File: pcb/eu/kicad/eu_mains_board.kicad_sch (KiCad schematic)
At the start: 10 parts, among them J1 2604-3102, J2 2604-3102, J3 TSM-102-02-L-SV

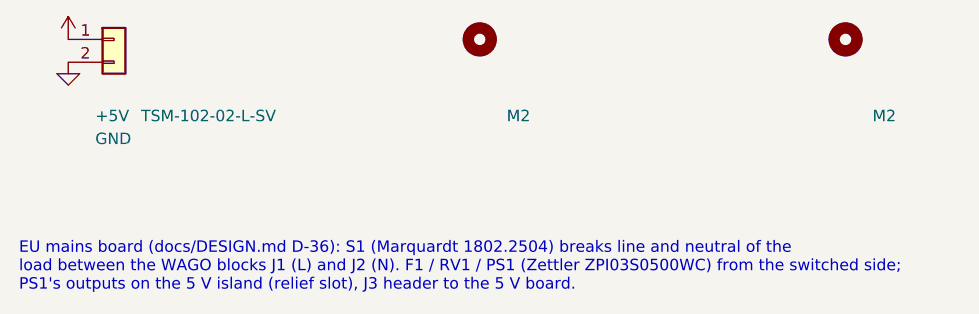
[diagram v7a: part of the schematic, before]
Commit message: Variants equal: na/eu/shared layout, shared part names, no default variant (D-125)
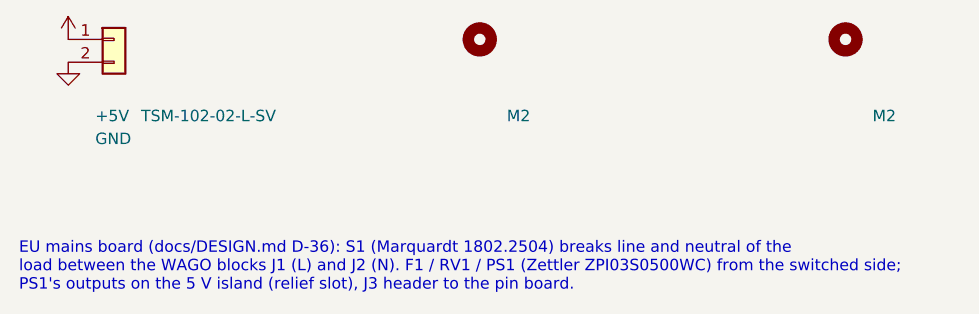
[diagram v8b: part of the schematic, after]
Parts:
- F1: footprint eu:Fuse_Schurter_UMT250 -> eu_mains:Fuse_Schurter_UMT250; symbol eu:Fuse -> eu_mains:Fuse
- J1, J2: footprint eu:WAGO_2604-3102_1x02_P5.00mm_Vertical -> eu_mains:WAGO_2604-3102_1x02_P5.00mm_Vertical; symbol eu:Screw_Terminal_01x02 -> eu_mains:Screw_Terminal_01x02
- J3: footprint eu:PinHeader_1x02_P2.54mm_Vertical_SMD_Pin1Left -> eu_mains:PinHeader_1x02_P2.54mm_Vertical_SMD_Pin1Left; symbol eu:Conn_01x02 -> eu_mains:Conn_01x02
- MH1, MH2, MH3: footprint eu:MountingHole_2.2mm_M2 -> eu_mains:MountingHole_2.2mm_M2; symbol eu:MountingHole -> eu_mains:MountingHole
- PS1: footprint eu:Converter_ACDC_Zettler_ZPI03_THT -> eu_mains:Converter_ACDC_Zettler_ZPI03_THT; symbol eu:ZPI03S0500WC -> eu_mains:ZPI03S0500WC
- RV1: footprint eu:Varistor_TDK_CU4032 -> eu_mains:Varistor_TDK_CU4032; symbol eu:Varistor -> eu_mains:Varistor
- S1: footprint eu:Rocker_DPST_Marquardt_1802.2504_E-Switch_RA412C1100 -> eu_mains:Rocker_DPST_Marquardt_1802.2504_E-Switch_RA412C1100; symbol eu:SW_DPST_Marquardt -> eu_mains:SW_DPST_Marquardt
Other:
- note added: "EU mains board (docs/DESIGN.md D-36): S1 (Marquardt 1802.2504) breaks line and neutral of the load between the WAGO blocks J1 (L) and J2 (N). F1 / RV1 / PS1 (Zettler ZPI03S0500WC) from the switched side; PS1's outputs on the 5 V island (relief slot), J3 header to the pin board."
- note removed: "EU mains board (docs/DESIGN.md D-36): S1 (Marquardt 1802.2504) breaks line and neutral of the load between the WAGO blocks J1 (L) and J2 (N). F1 / RV1 / PS1 (Zettler ZPI03S0500WC) from the switched side; PS1's outputs on the 5 V island (relief slot), J3 header to the 5 V board."
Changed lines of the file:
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@@
 		(rev "v0.6")
 		(company "smart-wallplate")
-		(comment 1 "Generated by pcb/eu/tools/gen_eu.py - edit eu_parts.py")
-	)
-	(symbol
-		(lib_id "eu:SW_DPST_Marquardt")
+		(comment 1 "Generated by pcb/eu/tools/gen_eu.py - edit parts_eu.py")
+	)
+	(symbol
+		(lib_id "eu_mains:SW_DPST_Marquardt")
 		(at 35.56 91.44 0)
 		(unit 1)
@@
 			)
 		)
-		(property "Footprint" "eu:Rocker_DPST_Marquardt_1802.2504_E-Switch_RA412C1100"
+		(property "Footprint" "eu_mains:Rocker_DPST_Marquardt_1802.2504_E-Switch_RA412C1100"
 			(at 35.56 91.44 0)
 			(effects
@@
 	)
 	(symbol
-		(lib_id "eu:Screw_Terminal_01x02")
+		(lib_id "eu_mains:Screw_Terminal_01x02")
 		(at 76.2 91.44 0)
 		(unit 1)
@@
 			)
 		)
-		(property "Footprint" "eu:WAGO_2604-3102_1x02_P5.00mm_Vertical"
+		(property "Footprint" "eu_mains:WAGO_2604-3102_1x02_P5.00mm_Vertical"
 			(at 76.2 91.44 0)
 			(effects
@@
 	)
 	(symbol
-		(lib_id "eu:Screw_Terminal_01x02")
+		(lib_id "eu_mains:Screw_Terminal_01x02")
 		(at 116.84 91.44 0)
 		(unit 1)
@@
 			)
 		)
-		(property "Footprint" "eu:WAGO_2604-3102_1x02_P5.00mm_Vertical"
+		(property "Footprint" "eu_mains:WAGO_2604-3102_1x02_P5.00mm_Vertical"
 			(at 116.84 91.44 0)
 			(effects
@@
 	)
 	(symbol
-		(lib_id "eu:Fuse")
+		(lib_id "eu_mains:Fuse")
 		(at 157.48 91.44 0)
 		(unit 1)
@@
 			)
 		)
-		(property "Footprint" "eu:Fuse_Schurter_UMT250"
+		(property "Footprint" "eu_mains:Fuse_Schurter_UMT250"
 			(at 157.48 91.44 0)
 			(effects
@@
 	)
 	(symbol
-		(lib_id "eu:Varistor")
+		(lib_id "eu_mains:Varistor")
 		(at 198.12 91.44 0)
 		(unit 1)
@@
 			)
 		)
-		(property "Footprint" "eu:Varistor_TDK_CU4032"
+		(property "Footprint" "eu_mains:Varistor_TDK_CU4032"
 			(at 198.12 91.44 0)
 			(effects
@@
 	)
 	(symbol
-		(lib_id "eu:ZPI03S0500WC")
+		(lib_id "eu_mains:ZPI03S0500WC")
 		(at 238.76 91.44 0)
 		(unit 1)
@@
 			)
 		)
-		(property "Footprint" "eu:Converter_ACDC_Zettler_ZPI03_THT"
+		(property "Footprint" "eu_mains:Converter_ACDC_Zettler_ZPI03_THT"
 			(at 238.76 91.44 0)
 			(effects
@@
 	)
 	(symbol
-		(lib_id "eu:+5V")
+		(lib_id "eu_mains:+5V")
 		(at 248.92 88.9 0)
 		(unit 1)
@@
 	)
 	(symbol
-		(lib_id "eu:GND")
+		(lib_id "eu_mains:GND")
 		(at 248.92 93.98 0)
 		(unit 1)
@@
 	)
 	(symbol
-		(lib_id "eu:Conn_01x02")
+		(lib_id "eu_mains:Conn_01x02")
 		(at 35.56 157.48 0)
 		(unit 1)
@@
 			)
 		)
-		(property "Footprint" "eu:PinHeader_1x02_P2.54mm_Vertical_SMD_Pin1Left"
+		(property "Footprint" "eu_mains:PinHeader_1x02_P2.54mm_Vertical_SMD_Pin1Left"
 			(at 35.56 157.48 0)
 			(effects
@@
 			)
 		)
-		(property "Description" "SMT pin header 1x2, 2.54 mm, 8.13 mm post, gold on post: 5 V to the 5 V board's pin socket (5 V island)"
+		(property "Description" "SMT pin header 1x2, 2.54 mm, 8.13 mm post, gold on post: 5 V to the pin board's pin socket (5 V island)"
 			(at 35.56 157.48 0)
 			(effects
@@
 	)
 	(symbol
-		(lib_id "eu:+5V")
+		(lib_id "eu_mains:+5V")
 		(at 30.48 157.48 0)
 		(unit 1)
@@
 	)
 	(symbol
-		(lib_id "eu:GND")
+		(lib_id "eu_mains:GND")
 		(at 30.48 160.02 0)
 		(unit 1)
@@
 	)
 	(symbol
-		(lib_id "eu:MountingHole")
+		(lib_id "eu_mains:MountingHole")
 		(at 76.2 157.48 0)
 		(unit 1)
@@
 			)
 		)
-		(property "Footprint" "eu:MountingHole_2.2mm_M2"
+		(property "Footprint" "eu_mains:MountingHole_2.2mm_M2"
 			(at 76.2 157.48 0)
 			(effects
@@
 			)
 		)
-		(property "Description" "M2 to the long cap boss"
+		(property "Description" "M2 to the long barrier boss"
 			(at 76.2 157.48 0)
 			(effects
@@
 	)
 	(symbol
-		(lib_id "eu:MountingHole")
+		(lib_id "eu_mains:MountingHole")
 		(at 116.84 157.48 0)
 		(unit 1)
@@
 			)
 		)
-		(property "Footprint" "eu:MountingHole_2.2mm_M2"
+		(property "Footprint" "eu_mains:MountingHole_2.2mm_M2"
 			(at 116.84 157.48 0)
 			(effects
@@
 			)
 		)
-		(property "Description" "M2 to the long cap boss"
+		(property "Description" "M2 to the long barrier boss"
 			(at 116.84 157.48 0)
 			(effects
@@
 	)
 	(symbol
-		(lib_id "eu:MountingHole")
+		(lib_id "eu_mains:MountingHole")
 		(at 157.48 157.48 0)
 		(unit 1)
@@
 			)
 		)
-		(property "Footprint" "eu:MountingHole_2.2mm_M2"
+		(property "Footprint" "eu_mains:MountingHole_2.2mm_M2"
 			(at 157.48 157.48 0)
 			(effects
@@
 			)
 		)
-		(property "Description" "M2 to the long cap boss"
+		(property "Description" "M2 to the long barrier boss"
 			(at 157.48 157.48 0)
 			(effects
@@
 	)
 	(symbol
-		(lib_id "eu:PWR_FLAG")
+		(lib_id "eu_mains:PWR_FLAG")
 		(at 35.56 50.8 0)
 		(unit 1)
@@
 	)
 	(symbol
-		(lib_id "eu:PWR_FLAG")
+		(lib_id "eu_mains:PWR_FLAG")
 		(at 66.04 50.8 0)
 		(unit 1)
@@
 	)
 	(symbol
-		(lib_id "eu:PWR_FLAG")
+		(lib_id "eu_mains:PWR_FLAG")
 		(at 96.52 50.8 0)
 		(unit 1)
@@
 	)
 	(symbol
-		(lib_id "eu:PWR_FLAG")
+		(lib_id "eu_mains:PWR_FLAG")
 		(at 127 50.8 0)
 		(unit 1)
@@
 		)
 	)
-	(text "EU mains board (docs/DESIGN.md D-36): S1 (Marquardt 1802.2504) breaks line and neutral of the\nload between the WAGO blocks J1 (L) and J2 (N). F1 / RV1 / PS1 (Zettler ZPI03S0500WC) from the switched side;\nPS1's outputs on the 5 V island (relief slot), J3 header to the 5 V board."
+	(text "EU mains board (docs/DESIGN.md D-36): S1 (Marquardt 1802.2504) breaks line and neutral of the\nload between the WAGO blocks J1 (L) and J2 (N). F1 / RV1 / PS1 (Zettler ZPI03S0500WC) from the switched side;\nPS1's outputs on the 5 V island (relief slot), J3 header to the pin board."
 		(exclude_from_sim no)
 		(at 25 180 0)
